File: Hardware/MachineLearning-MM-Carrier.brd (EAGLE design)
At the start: 58.4 x 54.6 mm, 124 parts, among them J11 microSD, J2 JTAG, J3 QWIIC_RIGHT_ANGLE, J9 MICROMOD-2222-C, U1 BME280, U2 VEML6075, U5 AP7361C-33FGE

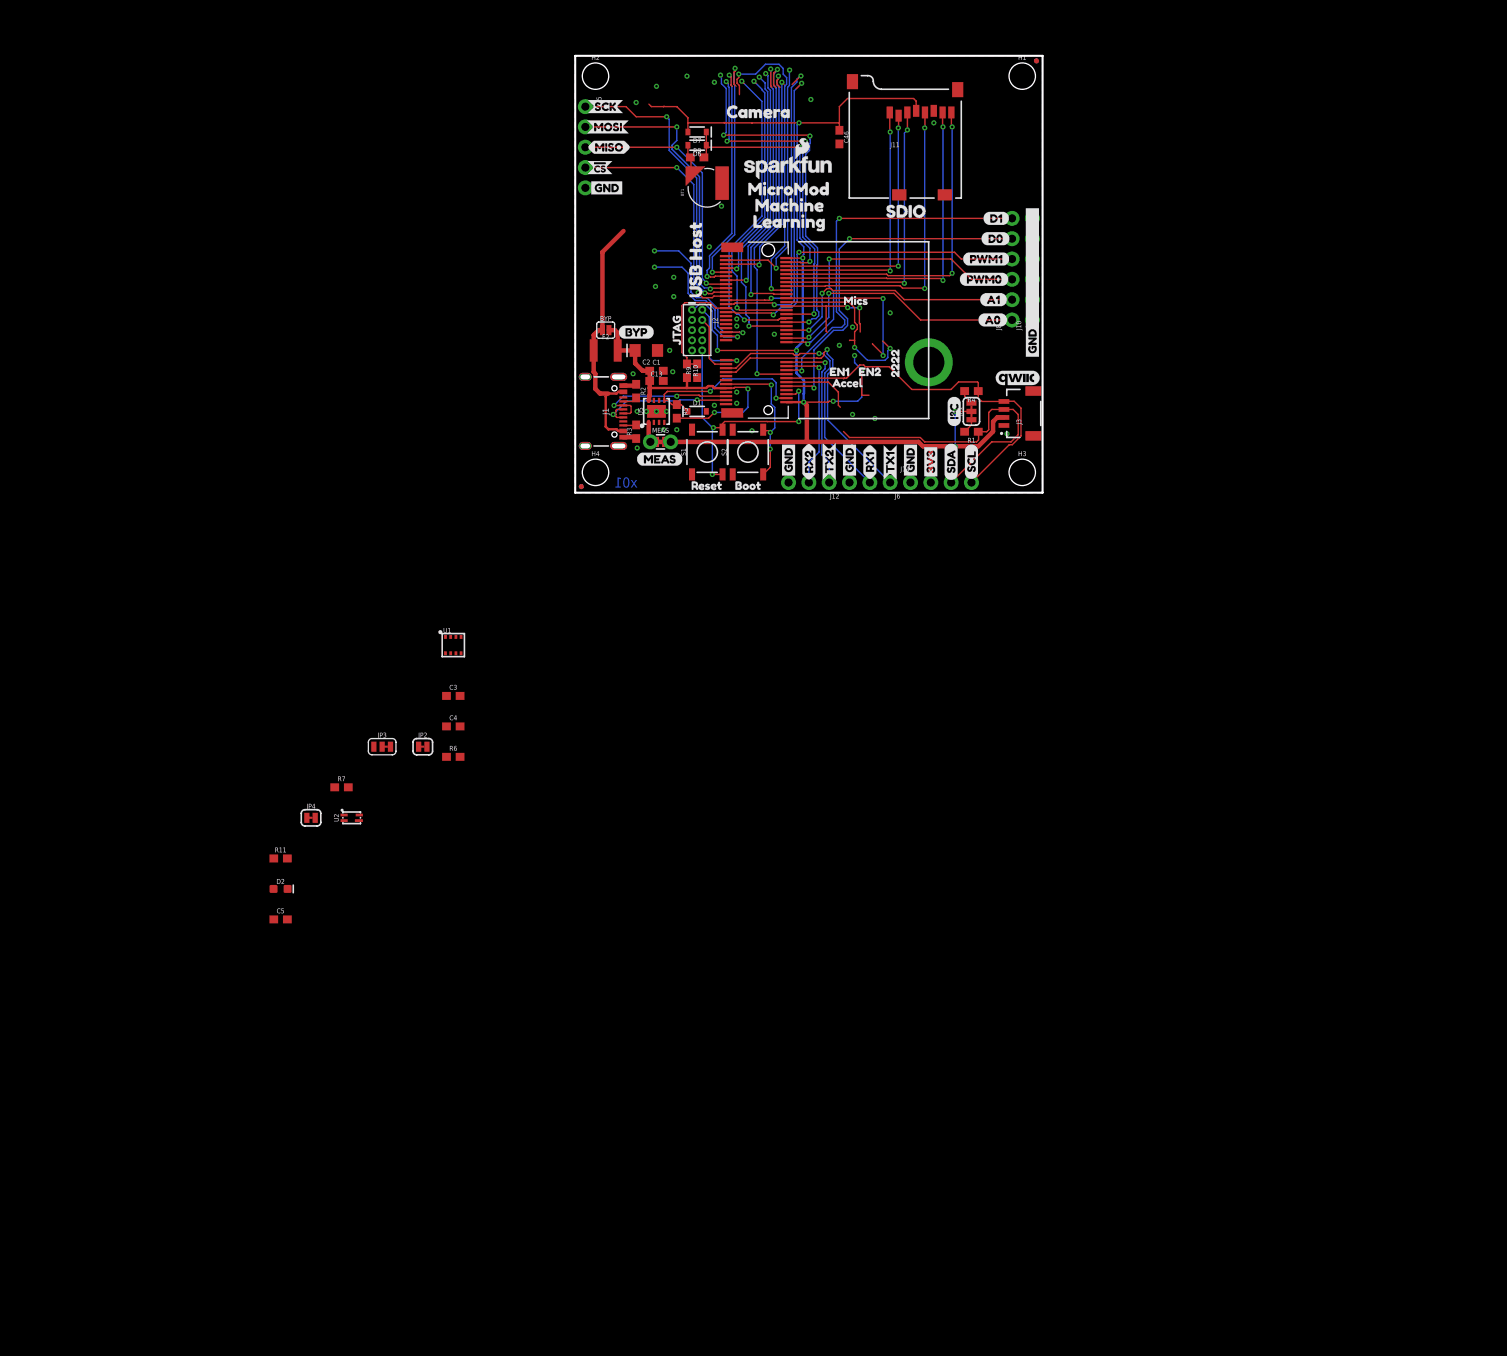
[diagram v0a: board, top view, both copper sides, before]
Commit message: Added connector for soil moisture sensor
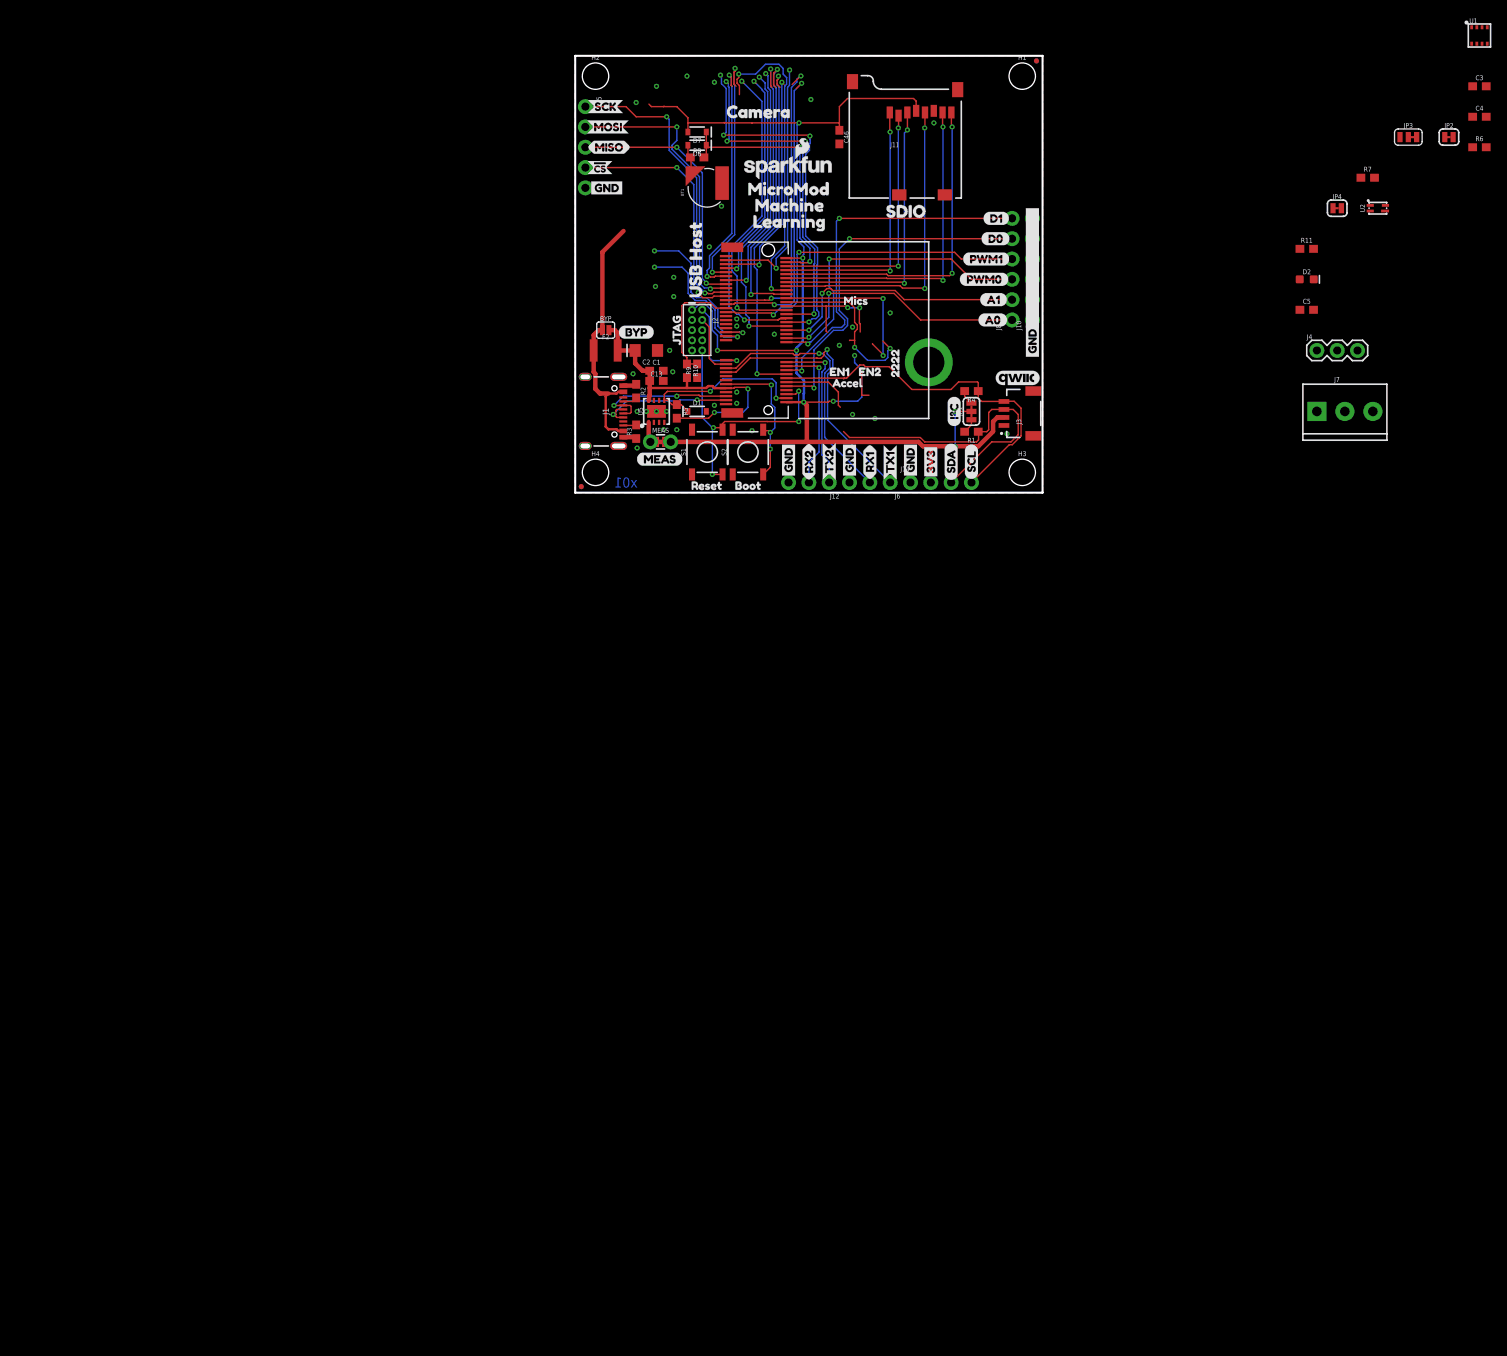
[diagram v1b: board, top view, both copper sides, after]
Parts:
- added J4: 455-1750-1-ND, SparkFun-Connectors:1X03
- added J7: (no value), SparkFun-Connectors:SCREWTERMINAL-3.5MM-3
- moved C3 149.2 mm to (113.0, 50.8)
- moved C4 149.2 mm to (113.0, 47.0)
- moved JP2 149.2 mm to (109.2, 44.5)
- moved JP3 149.2 mm to (104.1, 44.5)
- moved JP4 149.2 mm to (95.2, 35.6)
- moved R6 149.2 mm to (113.0, 43.2)
- moved R7 149.2 mm to (99.1, 39.4)
- moved U1 149.2 mm to (113.0, 57.1)
- moved U2 149.2 mm to (100.3, 35.6)
- moved C5 149.2 mm to (91.4, 22.9)
- moved D2 149.2 mm to (91.4, 26.7)
- moved R11 149.2 mm to (91.4, 30.5)
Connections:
- new net SOIL_MOIST_SIG: J4.1, J7.3
- net 3.3V: now also J4.3, J7.1
- net GND: now also J4.2, J7.2

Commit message: Added RJ11 connectors for weather station add-on
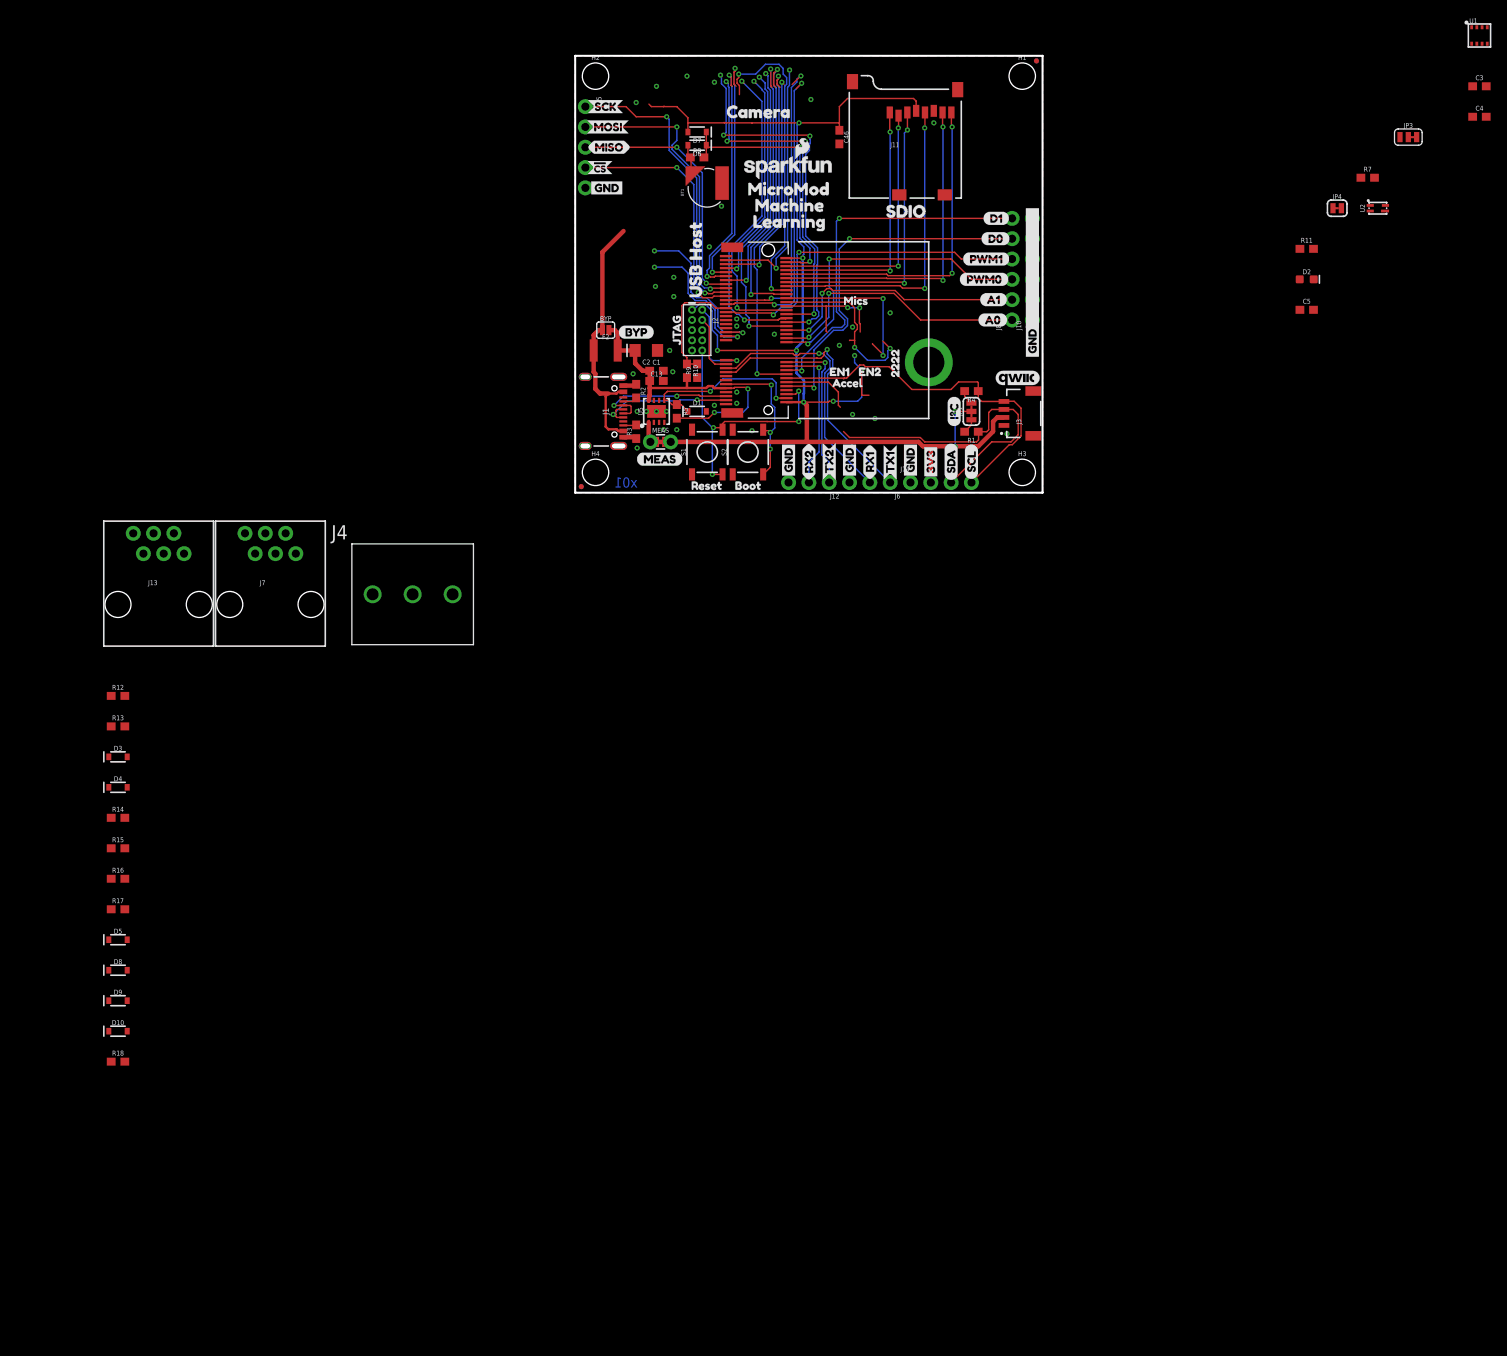
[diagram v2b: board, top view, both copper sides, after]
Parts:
- removed JP2: EN I2C MODE, SparkFun-Jumpers:SMT-JUMPER_2_NC_TRACE_SILK
- removed R6: 4.7k, SparkFun-Resistors:0603
- added D10, D3, D4, D5, D8, D9: 250mA/100V, SparkFun-DiscreteSemi:SOD-323
- added J13: RJ11 - WIND, SparkFun-Connectors:RJ11-6
- added R12, R13, R14, R15, R16, R17: 1k, SparkFun-Resistors:0603
- added R18: 4.7k, SparkFun-Resistors:0603
- J4: value 455-1750-1-ND -> (none); device SparkFun-Connectors:1X03 -> SparkFun-Connectors:LATCHTERMINAL-5MM-3
- J7: value (none) -> RJ11 - RAIN; device SparkFun-Connectors:SCREWTERMINAL-3.5MM-3 -> SparkFun-Connectors:RJ11-6
- moved J7 133.0 mm to (-38.1, -14.0)
- moved J4 117.1 mm to (-20.3, -12.7)
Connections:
- removed net N$5: JP2.1, R6.2
- new net 5V: D10.C, D3.C, D9.C, R18.2
- new net N$12: J13.5, R14.1
- new net N$13: J13.4, R15.1
- new net N$17: J13.3, R16.1
- new net N$18: J13.2, R17.1
- new net N$7: J7.4, R12.2
- new net N$9: J7.3, R13.2
- new net RAIN: D3.A, D4.C, R13.1
- new net RAIN2: J7.2
- new net RAIN5: J7.5
- new net WDIR: D5.C, D9.A, R17.2, R18.1
- new net WSPEED: D10.A, D8.C, R16.2
- net 3.3V: now also J4.1, U1.2; no longer J4.3, J7.1, JP2.2
- net GND: now also D4.A, D5.A, D8.A, R12.1, R14.2, R15.2; no longer J7.2
- net SOIL_MOIST_SIG: now also J4.3; no longer J4.1, J7.3
- net SPI_!CS!: no longer R6.1, U1.2

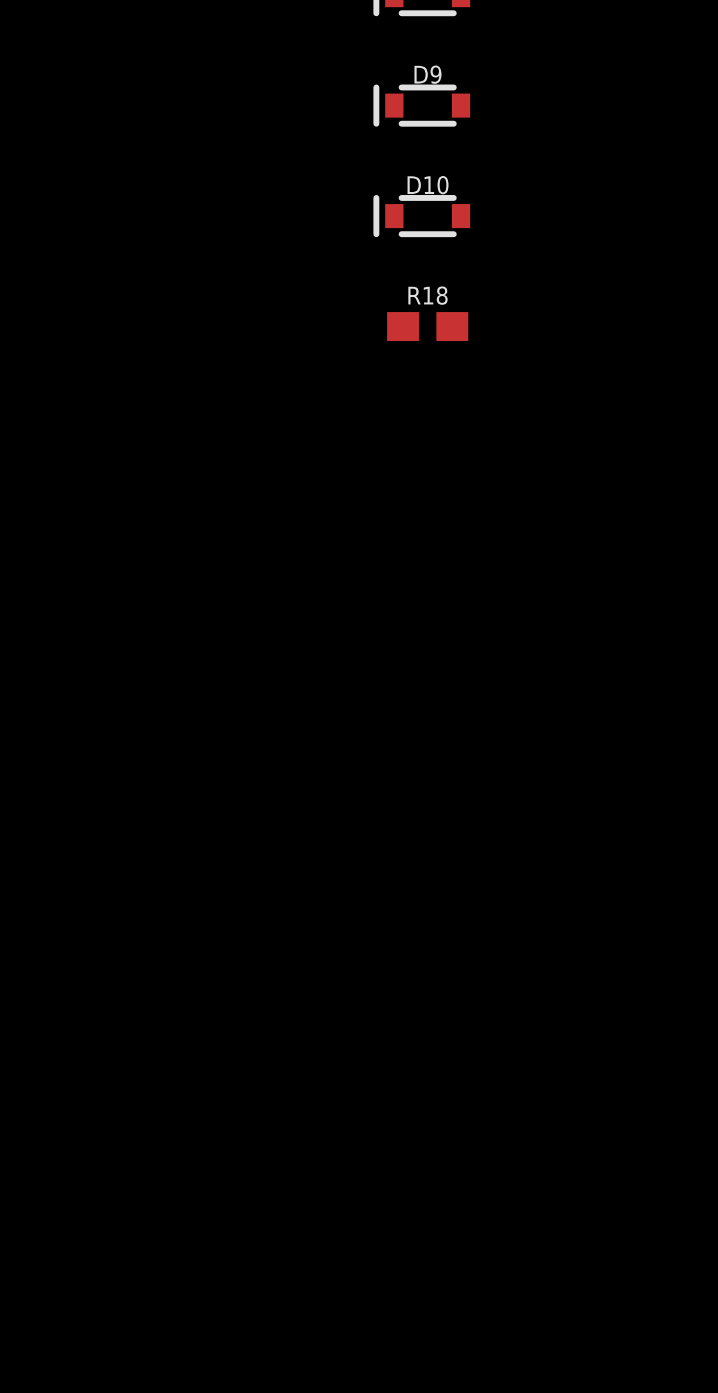
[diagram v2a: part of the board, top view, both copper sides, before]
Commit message: Added lightning detector block
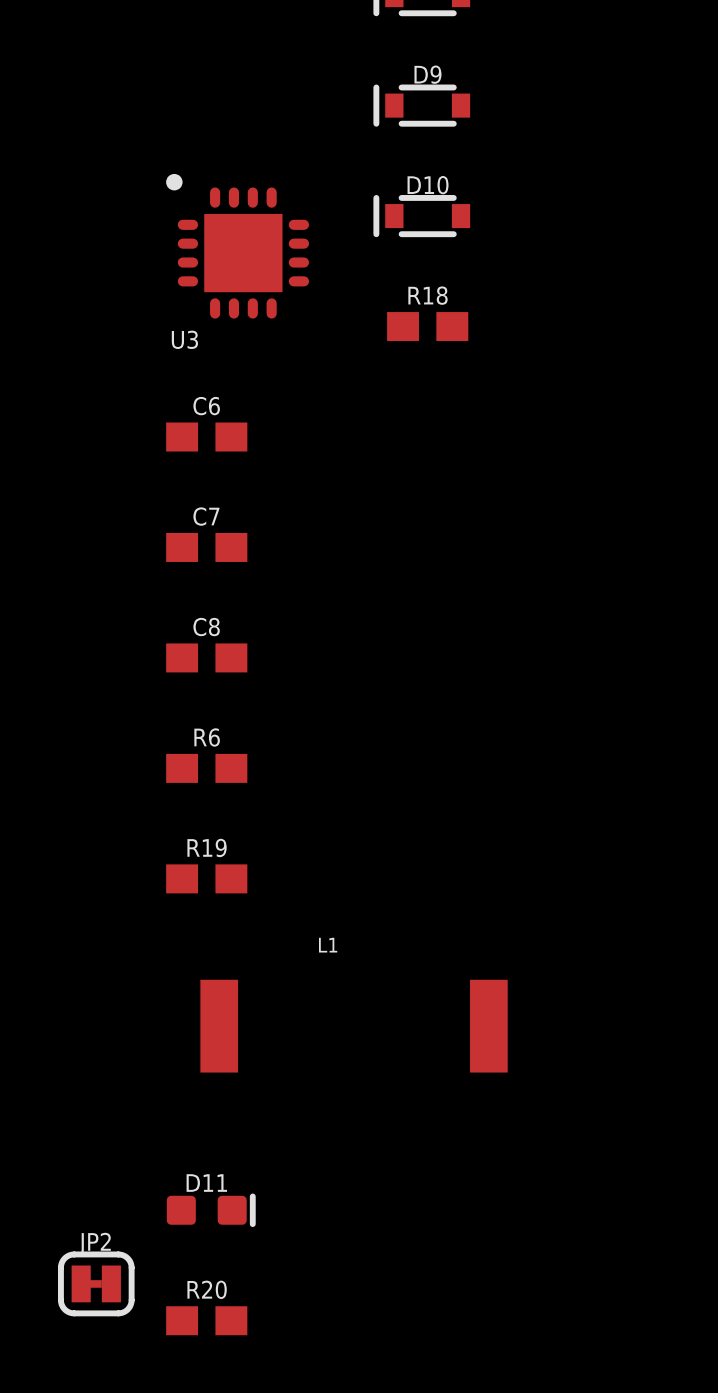
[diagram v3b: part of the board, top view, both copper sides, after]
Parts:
- added C6: 1.0uF, SparkFun-Capacitors:0603
- added C7: 10uF, SparkFun-Capacitors:0603
- added C8: 1nF, SparkFun-Capacitors:0603
- added D11: Yellow, SparkFun-LED:LED-0603
- added JP2: VIN LED ENABLE, SparkFun-Jumpers:SMT-JUMPER_2_NC_TRACE_SILK
- added L1: 100uH, SparkFun-Coils:MA5532-AE
- added R19, R6: 10k, SparkFun-Resistors:0603
- added R20: 1k, SparkFun-Resistors:0603
- added U3: AS3935, SparkFun-Sensors:16LD_MLPQ
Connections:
- new net INP: C8.1, L1.1, R6.2, U3.3
- new net LIGHTNING_INT: U3.10
- new net N$15: C7.1, U3.1
- new net N$16: D11.A, R20.1
- new net N$5: JP2.1, R20.2
- net 3.3V: now also C6.1, R19.2, U3.5, U3.6
- net GND: now also C6.2, C7.2, C8.2, D11.C, L1.2, R6.1, U3.17, U3.2, U3.4, U3.7, U3.9
- net SPI_!CS!: now also R19.1, U3.8
- net SPI_CLK: now also U3.11
- net SPI_MISO: now also U3.12
- net SPI_MOSI: now also U3.13
- net VIN: now also JP2.2
